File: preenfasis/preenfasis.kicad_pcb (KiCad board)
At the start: 2 copper layers, 25 x 40 mm, 24 parts, among them J1 SMA H, J2 SMA H, J3 SMA H, J4 SMA H

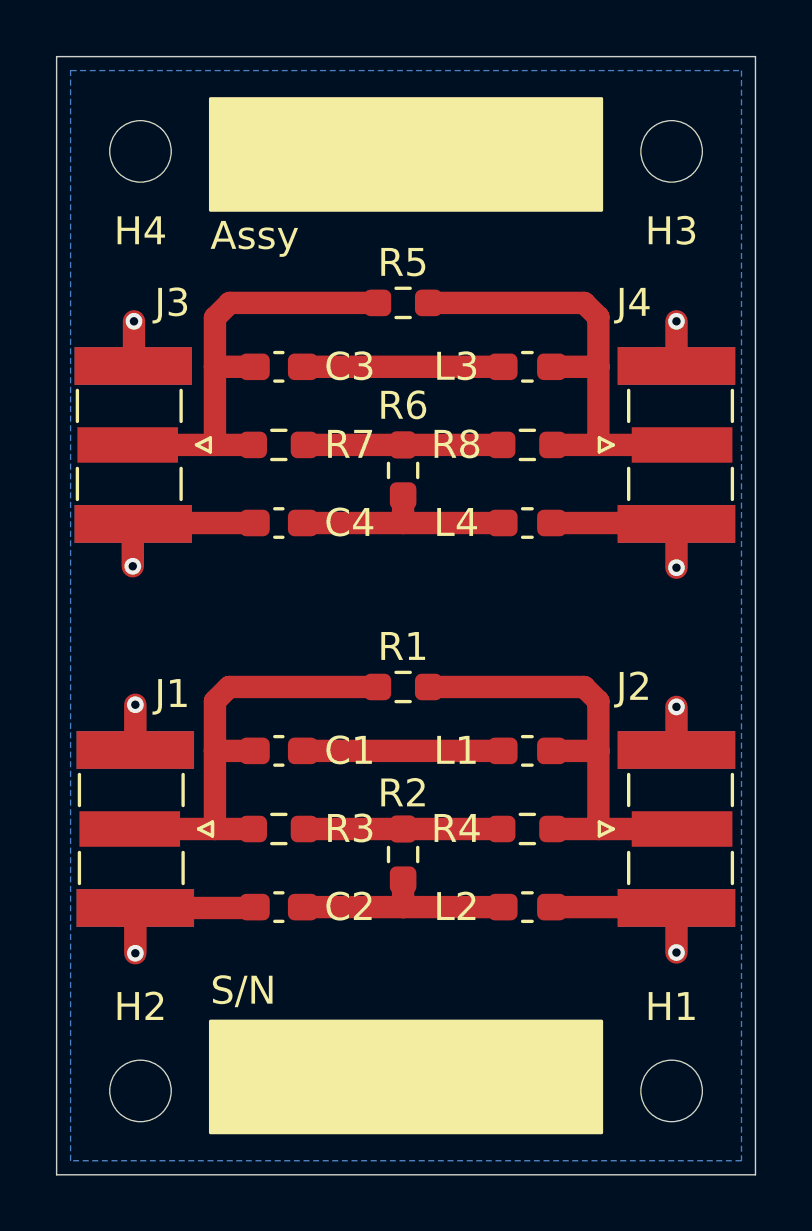
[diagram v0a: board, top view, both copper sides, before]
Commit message: Preenfasis v1.1
Se separaron los planos de tierra de ambas T
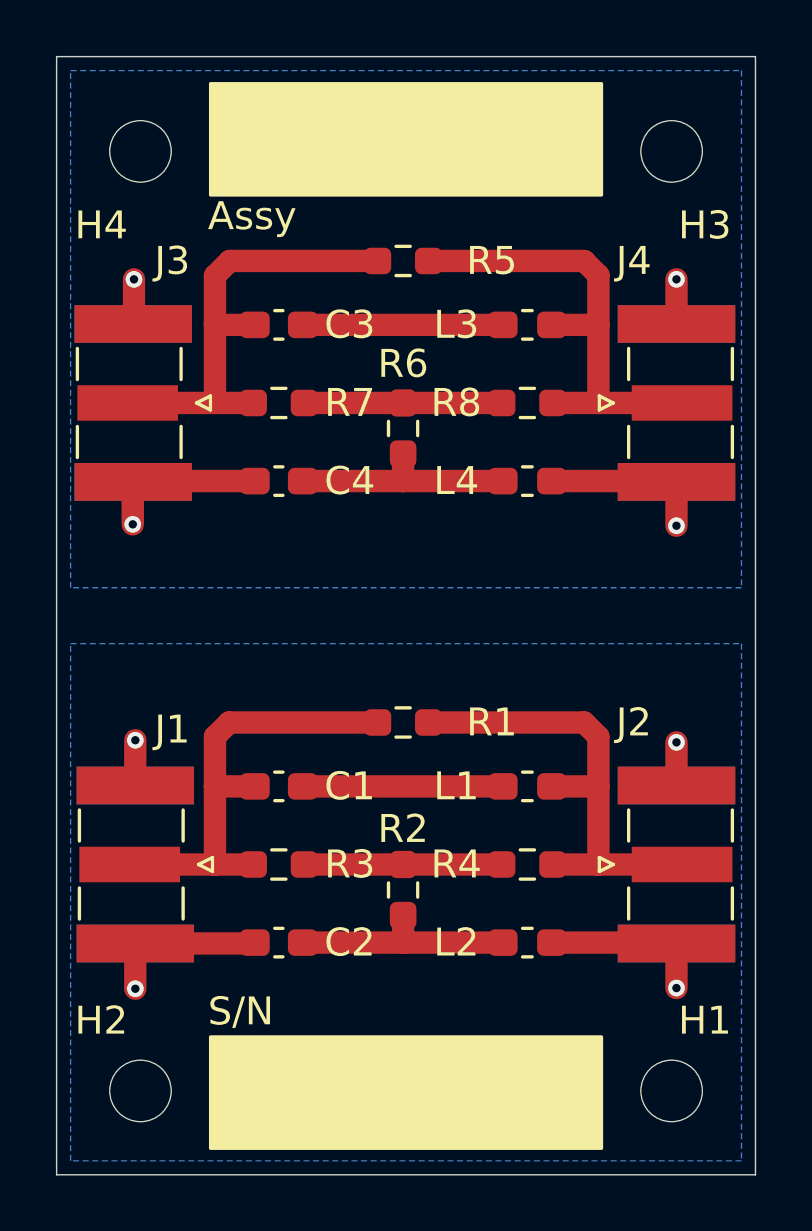
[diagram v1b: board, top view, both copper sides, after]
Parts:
- moved C3 1.50 mm to (108.0, 69.6)
- moved C4 1.50 mm to (108.0, 75.2)
- moved J3 1.50 mm to (102.7, 72.4)
- moved J4 1.50 mm to (122.2, 72.4)
- moved L3 1.50 mm to (116.8, 69.6)
- moved L4 1.50 mm to (116.8, 75.2)
- moved R5 1.50 mm to (112.4, 67.3)
- moved R6 1.50 mm to (112.4, 73.3)
- moved R7 1.50 mm to (108.0, 72.4)
- moved R8 1.50 mm to (116.8, 72.4)
- moved J1 1.27 mm to (102.8, 88.9)
- moved J2 1.27 mm to (122.2, 88.9)
- moved R3 1.27 mm to (108.0, 88.9)
- moved R4 1.27 mm to (116.8, 88.9)
- moved C1 1.27 mm to (108.0, 86.1)
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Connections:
- C4 pad 1: Net-(J1-Ext) -> Net-(J3-Ext)
- J3 pad 2: Net-(J1-Ext) -> Net-(J3-Ext)
- J4 pad 2: Net-(J1-Ext) -> Net-(J3-Ext)
- L4 pad 2: Net-(J1-Ext) -> Net-(J3-Ext)
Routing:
- net Net-(J1-Ext): track 30.8 -> 15.3 mm, vias 8 -> 4
- net Net-(J3-Ext): track 0.00 -> 15.6 mm, vias 0 -> 4
- added copper zone on B.Cu, net Net-(J3-Ext)
